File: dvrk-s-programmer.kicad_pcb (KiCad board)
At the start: 4 copper layers, 85.5 x 53 mm, 20 parts, among them J2 Conn_01x04, J3 Conn_02x05_Odd_Even, SW1 SW_SPDT, U1 STM32F103C8Tx, U3 XKTF-015-N

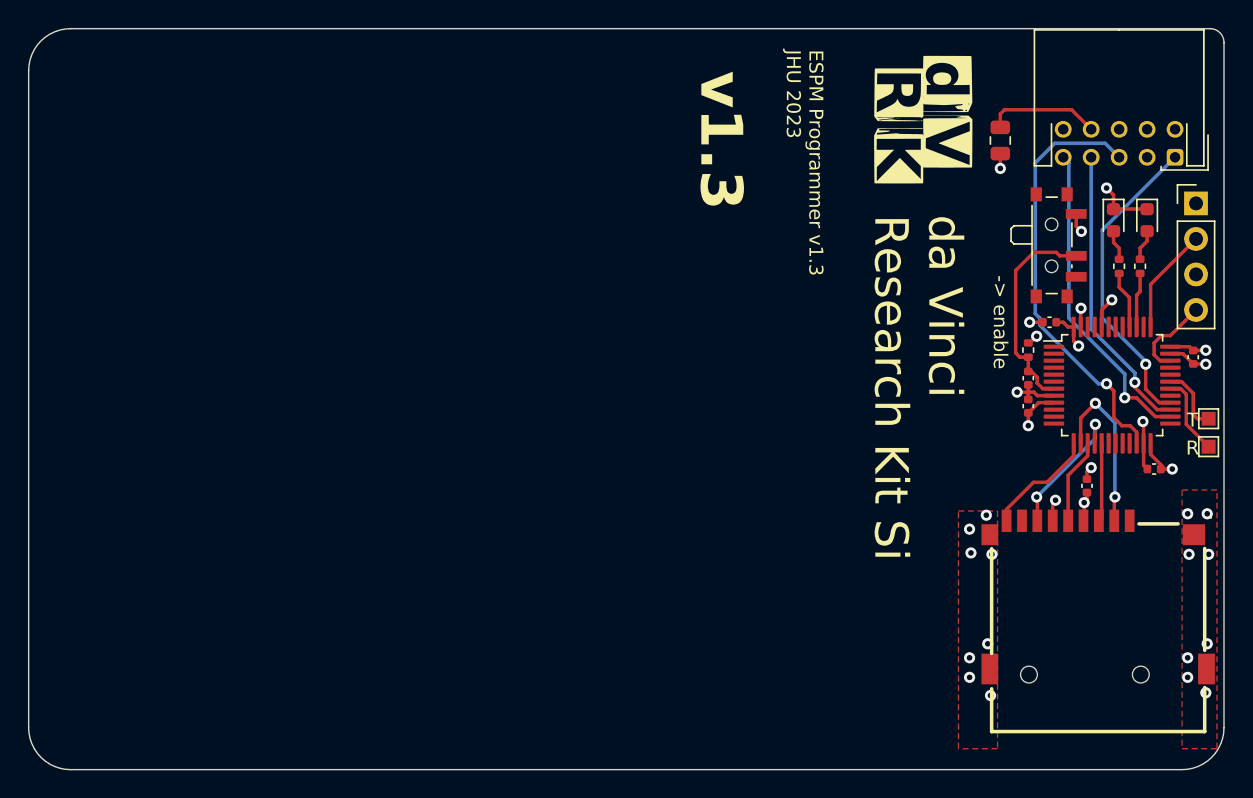
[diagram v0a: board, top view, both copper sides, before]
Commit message: added led array. changed microcontroller.
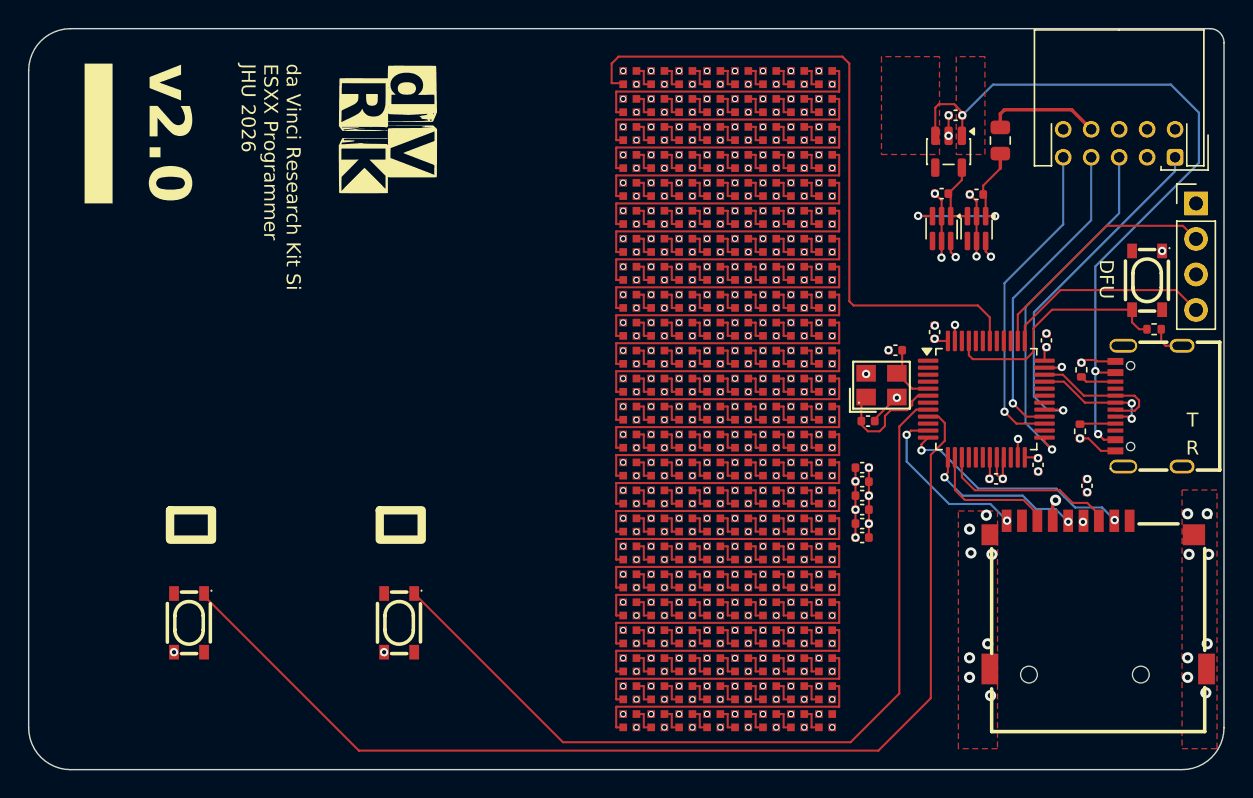
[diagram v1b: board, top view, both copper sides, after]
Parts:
- removed D1, D2: LED, LED_SMD:LED_0603_1608Metric
- removed R2, R3: 2.61k, Resistor_SMD:R_0402_1005Metric
- removed SW1: SW_SPDT, Button_Switch_SMD:SW_SPDT_PCM12
- removed TP1, TP2: TestPoint, TestPoint:TestPoint_Pad_1.0x1.0mm
- removed the U1 at (191.0, 137.0)
- added C11: 1uF, Capacitor_SMD:C_0402_1005Metric, F.Cu at (173.1, 142.9)
- added C12: 1uF, Capacitor_SMD:C_0402_1005Metric, F.Cu at (173.1, 143.9)
- added C13: 1uF, Capacitor_SMD:C_0402_1005Metric, F.Cu at (173.1, 144.9)
- added C14: 1uF, Capacitor_SMD:C_0402_1005Metric, F.Cu at (173.1, 145.9)
- added C15: 1uF, Capacitor_SMD:C_0402_1005Metric, F.Cu at (173.1, 146.9)
- added C16: 1uF, Capacitor_SMD:C_0402_1005Metric, F.Cu at (173.1, 147.9)
- added C2: 10pf, Capacitor_SMD:C_0402_1005Metric, F.Cu at (173.5, 139.6)
- added C5: 1uf, Capacitor_SMD:C_0402_1005Metric, F.Cu at (179.8, 117.7)
- added C8: 1uf, Capacitor_SMD:C_0402_1005Metric, F.Cu at (181.3, 123.4)
- added C9: 1uf, Capacitor_SMD:C_0402_1005Metric, F.Cu at (178.8, 123.3)
- added D10: SK6805-EC15, led-array-generator:SK6805-EC15, F.Cu at (156.5, 129.0)
- added D100: SK6805-EC15, led-array-generator:SK6805-EC15, F.Cu at (164.5, 117.0)
- added D101: SK6805-EC15, led-array-generator:SK6805-EC15, F.Cu at (164.5, 119.0)
- added D102: SK6805-EC15, led-array-generator:SK6805-EC15, F.Cu at (164.5, 121.0)
- added D103: SK6805-EC15, led-array-generator:SK6805-EC15, F.Cu at (164.5, 123.0)
- added D104: SK6805-EC15, led-array-generator:SK6805-EC15, F.Cu at (164.5, 125.0)
- added D105: SK6805-EC15, led-array-generator:SK6805-EC15, F.Cu at (164.5, 127.0)
- added D106: SK6805-EC15, led-array-generator:SK6805-EC15, F.Cu at (164.5, 129.0)
- added D107: SK6805-EC15, led-array-generator:SK6805-EC15, F.Cu at (164.5, 131.0)
- added D108: SK6805-EC15, led-array-generator:SK6805-EC15, F.Cu at (164.5, 133.0)
- added D109: SK6805-EC15, led-array-generator:SK6805-EC15, F.Cu at (164.5, 135.0)
- added D11: SK6805-EC15, led-array-generator:SK6805-EC15, F.Cu at (156.5, 131.0)
- added D110: SK6805-EC15, led-array-generator:SK6805-EC15, F.Cu at (164.5, 137.0)
- added D111: SK6805-EC15, led-array-generator:SK6805-EC15, F.Cu at (164.5, 139.0)
- added D112: SK6805-EC15, led-array-generator:SK6805-EC15, F.Cu at (164.5, 141.0)
- added D113: SK6805-EC15, led-array-generator:SK6805-EC15, F.Cu at (164.5, 143.0)
- added D114: SK6805-EC15, led-array-generator:SK6805-EC15, F.Cu at (164.5, 145.0)
- added D115: SK6805-EC15, led-array-generator:SK6805-EC15, F.Cu at (164.5, 147.0)
- added D116: SK6805-EC15, led-array-generator:SK6805-EC15, F.Cu at (164.5, 149.0)
- added D117: SK6805-EC15, led-array-generator:SK6805-EC15, F.Cu at (164.5, 151.0)
- added D118: SK6805-EC15, led-array-generator:SK6805-EC15, F.Cu at (164.5, 153.0)
- added D119: SK6805-EC15, led-array-generator:SK6805-EC15, F.Cu at (164.5, 155.0)
- added D12: SK6805-EC15, led-array-generator:SK6805-EC15, F.Cu at (156.5, 133.0)
- added D120: SK6805-EC15, led-array-generator:SK6805-EC15, F.Cu at (164.5, 157.0)
- added D121: SK6805-EC15, led-array-generator:SK6805-EC15, F.Cu at (164.5, 159.0)
- added D122: SK6805-EC15, led-array-generator:SK6805-EC15, F.Cu at (164.5, 161.0)
- added D123: SK6805-EC15, led-array-generator:SK6805-EC15, F.Cu at (166.5, 115.0)
- added D124: SK6805-EC15, led-array-generator:SK6805-EC15, F.Cu at (166.5, 117.0)
- added D125: SK6805-EC15, led-array-generator:SK6805-EC15, F.Cu at (166.5, 119.0)
- added D126: SK6805-EC15, led-array-generator:SK6805-EC15, F.Cu at (166.5, 121.0)
- added D127: SK6805-EC15, led-array-generator:SK6805-EC15, F.Cu at (166.5, 123.0)
- added D128: SK6805-EC15, led-array-generator:SK6805-EC15, F.Cu at (166.5, 125.0)
- added D129: SK6805-EC15, led-array-generator:SK6805-EC15, F.Cu at (166.5, 127.0)
- added D13: SK6805-EC15, led-array-generator:SK6805-EC15, F.Cu at (156.5, 135.0)
- added D130: SK6805-EC15, led-array-generator:SK6805-EC15, F.Cu at (166.5, 129.0)
- added D131: SK6805-EC15, led-array-generator:SK6805-EC15, F.Cu at (166.5, 131.0)
- added D132: SK6805-EC15, led-array-generator:SK6805-EC15, F.Cu at (166.5, 133.0)
- added D133: SK6805-EC15, led-array-generator:SK6805-EC15, F.Cu at (166.5, 135.0)
- added D134: SK6805-EC15, led-array-generator:SK6805-EC15, F.Cu at (166.5, 137.0)
- added D135: SK6805-EC15, led-array-generator:SK6805-EC15, F.Cu at (166.5, 139.0)
- added D136: SK6805-EC15, led-array-generator:SK6805-EC15, F.Cu at (166.5, 141.0)
- added D137: SK6805-EC15, led-array-generator:SK6805-EC15, F.Cu at (166.5, 143.0)
- added D138: SK6805-EC15, led-array-generator:SK6805-EC15, F.Cu at (166.5, 145.0)
- added D139: SK6805-EC15, led-array-generator:SK6805-EC15, F.Cu at (166.5, 147.0)
- added D14: SK6805-EC15, led-array-generator:SK6805-EC15, F.Cu at (156.5, 137.0)
- added D140: SK6805-EC15, led-array-generator:SK6805-EC15, F.Cu at (166.5, 149.0)
- added D141: SK6805-EC15, led-array-generator:SK6805-EC15, F.Cu at (166.5, 151.0)
- added D142: SK6805-EC15, led-array-generator:SK6805-EC15, F.Cu at (166.5, 153.0)
- added D143: SK6805-EC15, led-array-generator:SK6805-EC15, F.Cu at (166.5, 155.0)
- added D144: SK6805-EC15, led-array-generator:SK6805-EC15, F.Cu at (166.5, 157.0)
- added D145: SK6805-EC15, led-array-generator:SK6805-EC15, F.Cu at (166.5, 159.0)
- added D146: SK6805-EC15, led-array-generator:SK6805-EC15, F.Cu at (166.5, 161.0)
- added D147: SK6805-EC15, led-array-generator:SK6805-EC15, F.Cu at (168.5, 115.0)
- added D148: SK6805-EC15, led-array-generator:SK6805-EC15, F.Cu at (168.5, 117.0)
- added D149: SK6805-EC15, led-array-generator:SK6805-EC15, F.Cu at (168.5, 119.0)
- added D15: SK6805-EC15, led-array-generator:SK6805-EC15, F.Cu at (156.5, 139.0)
- added D150: SK6805-EC15, led-array-generator:SK6805-EC15, F.Cu at (168.5, 121.0)
- added D151: SK6805-EC15, led-array-generator:SK6805-EC15, F.Cu at (168.5, 123.0)
- added D152: SK6805-EC15, led-array-generator:SK6805-EC15, F.Cu at (168.5, 125.0)
- added D153: SK6805-EC15, led-array-generator:SK6805-EC15, F.Cu at (168.5, 127.0)
- added D154: SK6805-EC15, led-array-generator:SK6805-EC15, F.Cu at (168.5, 129.0)
- added D155: SK6805-EC15, led-array-generator:SK6805-EC15, F.Cu at (168.5, 131.0)
- added D156: SK6805-EC15, led-array-generator:SK6805-EC15, F.Cu at (168.5, 133.0)
- added D157: SK6805-EC15, led-array-generator:SK6805-EC15, F.Cu at (168.5, 135.0)
- added D158: SK6805-EC15, led-array-generator:SK6805-EC15, F.Cu at (168.5, 137.0)
- added D159: SK6805-EC15, led-array-generator:SK6805-EC15, F.Cu at (168.5, 139.0)
- added D16: SK6805-EC15, led-array-generator:SK6805-EC15, F.Cu at (156.5, 141.0)
- added D160: SK6805-EC15, led-array-generator:SK6805-EC15, F.Cu at (168.5, 141.0)
- added D161: SK6805-EC15, led-array-generator:SK6805-EC15, F.Cu at (168.5, 143.0)
- added D162: SK6805-EC15, led-array-generator:SK6805-EC15, F.Cu at (168.5, 145.0)
- added D163: SK6805-EC15, led-array-generator:SK6805-EC15, F.Cu at (168.5, 147.0)
- added D164: SK6805-EC15, led-array-generator:SK6805-EC15, F.Cu at (168.5, 149.0)
- added D165: SK6805-EC15, led-array-generator:SK6805-EC15, F.Cu at (168.5, 151.0)
- added D166: SK6805-EC15, led-array-generator:SK6805-EC15, F.Cu at (168.5, 153.0)
- added D167: SK6805-EC15, led-array-generator:SK6805-EC15, F.Cu at (168.5, 155.0)
- added D168: SK6805-EC15, led-array-generator:SK6805-EC15, F.Cu at (168.5, 157.0)
- added D169: SK6805-EC15, led-array-generator:SK6805-EC15, F.Cu at (168.5, 159.0)
- added D17: SK6805-EC15, led-array-generator:SK6805-EC15, F.Cu at (156.5, 143.0)
- added D170: SK6805-EC15, led-array-generator:SK6805-EC15, F.Cu at (168.5, 161.0)
- added D171: SK6805-EC15, led-array-generator:SK6805-EC15, F.Cu at (170.5, 115.0)
- added D172: SK6805-EC15, led-array-generator:SK6805-EC15, F.Cu at (170.5, 117.0)
- added D173: SK6805-EC15, led-array-generator:SK6805-EC15, F.Cu at (170.5, 119.0)
- added D174: SK6805-EC15, led-array-generator:SK6805-EC15, F.Cu at (170.5, 121.0)
- added D175: SK6805-EC15, led-array-generator:SK6805-EC15, F.Cu at (170.5, 123.0)
- added D176: SK6805-EC15, led-array-generator:SK6805-EC15, F.Cu at (170.5, 125.0)
- added D177: SK6805-EC15, led-array-generator:SK6805-EC15, F.Cu at (170.5, 127.0)
- added D178: SK6805-EC15, led-array-generator:SK6805-EC15, F.Cu at (170.5, 129.0)
- added D179: SK6805-EC15, led-array-generator:SK6805-EC15, F.Cu at (170.5, 131.0)
- added D18: SK6805-EC15, led-array-generator:SK6805-EC15, F.Cu at (156.5, 145.0)
- added D180: SK6805-EC15, led-array-generator:SK6805-EC15, F.Cu at (170.5, 133.0)
- added D181: SK6805-EC15, led-array-generator:SK6805-EC15, F.Cu at (170.5, 135.0)
- added D182: SK6805-EC15, led-array-generator:SK6805-EC15, F.Cu at (170.5, 137.0)
- added D183: SK6805-EC15, led-array-generator:SK6805-EC15, F.Cu at (170.5, 139.0)
- added D184: SK6805-EC15, led-array-generator:SK6805-EC15, F.Cu at (170.5, 141.0)
- added D185: SK6805-EC15, led-array-generator:SK6805-EC15, F.Cu at (170.5, 143.0)
- added D186: SK6805-EC15, led-array-generator:SK6805-EC15, F.Cu at (170.5, 145.0)
- added D187: SK6805-EC15, led-array-generator:SK6805-EC15, F.Cu at (170.5, 147.0)
- added D188: SK6805-EC15, led-array-generator:SK6805-EC15, F.Cu at (170.5, 149.0)
- added D189: SK6805-EC15, led-array-generator:SK6805-EC15, F.Cu at (170.5, 151.0)
- added D19: SK6805-EC15, led-array-generator:SK6805-EC15, F.Cu at (156.5, 147.0)
- added D190: SK6805-EC15, led-array-generator:SK6805-EC15, F.Cu at (170.5, 153.0)
- added D191: SK6805-EC15, led-array-generator:SK6805-EC15, F.Cu at (170.5, 155.0)
- added D192: SK6805-EC15, led-array-generator:SK6805-EC15, F.Cu at (170.5, 157.0)
- added D193: SK6805-EC15, led-array-generator:SK6805-EC15, F.Cu at (170.5, 159.0)
- added D194: SK6805-EC15, led-array-generator:SK6805-EC15, F.Cu at (170.5, 161.0)
- added D20: SK6805-EC15, led-array-generator:SK6805-EC15, F.Cu at (156.5, 149.0)
- added D21: SK6805-EC15, led-array-generator:SK6805-EC15, F.Cu at (156.5, 151.0)
- added D22: SK6805-EC15, led-array-generator:SK6805-EC15, F.Cu at (156.5, 153.0)
- added D23: SK6805-EC15, led-array-generator:SK6805-EC15, F.Cu at (156.5, 155.0)
- added D24: SK6805-EC15, led-array-generator:SK6805-EC15, F.Cu at (156.5, 157.0)
- added D25: SK6805-EC15, led-array-generator:SK6805-EC15, F.Cu at (156.5, 159.0)
- added D26: SK6805-EC15, led-array-generator:SK6805-EC15, F.Cu at (156.5, 161.0)
- added D27: SK6805-EC15, led-array-generator:SK6805-EC15, F.Cu at (158.5, 115.0)
- added D28: SK6805-EC15, led-array-generator:SK6805-EC15, F.Cu at (158.5, 117.0)
- added D29: SK6805-EC15, led-array-generator:SK6805-EC15, F.Cu at (158.5, 119.0)
- added D3: SK6805-EC15, led-array-generator:SK6805-EC15, F.Cu at (156.5, 115.0)
- added D30: SK6805-EC15, led-array-generator:SK6805-EC15, F.Cu at (158.5, 121.0)
- added D31: SK6805-EC15, led-array-generator:SK6805-EC15, F.Cu at (158.5, 123.0)
- added D32: SK6805-EC15, led-array-generator:SK6805-EC15, F.Cu at (158.5, 125.0)
- added D33: SK6805-EC15, led-array-generator:SK6805-EC15, F.Cu at (158.5, 127.0)
- added D34: SK6805-EC15, led-array-generator:SK6805-EC15, F.Cu at (158.5, 129.0)
- added D35: SK6805-EC15, led-array-generator:SK6805-EC15, F.Cu at (158.5, 131.0)
- added D36: SK6805-EC15, led-array-generator:SK6805-EC15, F.Cu at (158.5, 133.0)
- added D37: SK6805-EC15, led-array-generator:SK6805-EC15, F.Cu at (158.5, 135.0)
- added D38: SK6805-EC15, led-array-generator:SK6805-EC15, F.Cu at (158.5, 137.0)
- added D39: SK6805-EC15, led-array-generator:SK6805-EC15, F.Cu at (158.5, 139.0)
- added D4: SK6805-EC15, led-array-generator:SK6805-EC15, F.Cu at (156.5, 117.0)
- added D40: SK6805-EC15, led-array-generator:SK6805-EC15, F.Cu at (158.5, 141.0)
- added D41: SK6805-EC15, led-array-generator:SK6805-EC15, F.Cu at (158.5, 143.0)
- added D42: SK6805-EC15, led-array-generator:SK6805-EC15, F.Cu at (158.5, 145.0)
- added D43: SK6805-EC15, led-array-generator:SK6805-EC15, F.Cu at (158.5, 147.0)
- added D44: SK6805-EC15, led-array-generator:SK6805-EC15, F.Cu at (158.5, 149.0)
- added D45: SK6805-EC15, led-array-generator:SK6805-EC15, F.Cu at (158.5, 151.0)
- added D46: SK6805-EC15, led-array-generator:SK6805-EC15, F.Cu at (158.5, 153.0)
- added D47: SK6805-EC15, led-array-generator:SK6805-EC15, F.Cu at (158.5, 155.0)
- added D48: SK6805-EC15, led-array-generator:SK6805-EC15, F.Cu at (158.5, 157.0)
- added D49: SK6805-EC15, led-array-generator:SK6805-EC15, F.Cu at (158.5, 159.0)
- added D5: SK6805-EC15, led-array-generator:SK6805-EC15, F.Cu at (156.5, 119.0)
- added D50: SK6805-EC15, led-array-generator:SK6805-EC15, F.Cu at (158.5, 161.0)
- added D51: SK6805-EC15, led-array-generator:SK6805-EC15, F.Cu at (160.5, 115.0)
- added D52: SK6805-EC15, led-array-generator:SK6805-EC15, F.Cu at (160.5, 117.0)
- added D53: SK6805-EC15, led-array-generator:SK6805-EC15, F.Cu at (160.5, 119.0)
- added D54: SK6805-EC15, led-array-generator:SK6805-EC15, F.Cu at (160.5, 121.0)
- added D55: SK6805-EC15, led-array-generator:SK6805-EC15, F.Cu at (160.5, 123.0)
- added D56: SK6805-EC15, led-array-generator:SK6805-EC15, F.Cu at (160.5, 125.0)
- added D57: SK6805-EC15, led-array-generator:SK6805-EC15, F.Cu at (160.5, 127.0)
- added D58: SK6805-EC15, led-array-generator:SK6805-EC15, F.Cu at (160.5, 129.0)
- added D59: SK6805-EC15, led-array-generator:SK6805-EC15, F.Cu at (160.5, 131.0)
- added D6: SK6805-EC15, led-array-generator:SK6805-EC15, F.Cu at (156.5, 121.0)
- added D60: SK6805-EC15, led-array-generator:SK6805-EC15, F.Cu at (160.5, 133.0)
- added D61: SK6805-EC15, led-array-generator:SK6805-EC15, F.Cu at (160.5, 135.0)
- added D62: SK6805-EC15, led-array-generator:SK6805-EC15, F.Cu at (160.5, 137.0)
- added D63: SK6805-EC15, led-array-generator:SK6805-EC15, F.Cu at (160.5, 139.0)
- added D64: SK6805-EC15, led-array-generator:SK6805-EC15, F.Cu at (160.5, 141.0)
- added D65: SK6805-EC15, led-array-generator:SK6805-EC15, F.Cu at (160.5, 143.0)
- added D66: SK6805-EC15, led-array-generator:SK6805-EC15, F.Cu at (160.5, 145.0)
- added D67: SK6805-EC15, led-array-generator:SK6805-EC15, F.Cu at (160.5, 147.0)
- added D68: SK6805-EC15, led-array-generator:SK6805-EC15, F.Cu at (160.5, 149.0)
- added D69: SK6805-EC15, led-array-generator:SK6805-EC15, F.Cu at (160.5, 151.0)
- added D7: SK6805-EC15, led-array-generator:SK6805-EC15, F.Cu at (156.5, 123.0)
- added D70: SK6805-EC15, led-array-generator:SK6805-EC15, F.Cu at (160.5, 153.0)
- added D71: SK6805-EC15, led-array-generator:SK6805-EC15, F.Cu at (160.5, 155.0)
- added D72: SK6805-EC15, led-array-generator:SK6805-EC15, F.Cu at (160.5, 157.0)
- added D73: SK6805-EC15, led-array-generator:SK6805-EC15, F.Cu at (160.5, 159.0)
- added D74: SK6805-EC15, led-array-generator:SK6805-EC15, F.Cu at (160.5, 161.0)
- added D75: SK6805-EC15, led-array-generator:SK6805-EC15, F.Cu at (162.5, 115.0)
- added D76: SK6805-EC15, led-array-generator:SK6805-EC15, F.Cu at (162.5, 117.0)
- added D77: SK6805-EC15, led-array-generator:SK6805-EC15, F.Cu at (162.5, 119.0)
- added D78: SK6805-EC15, led-array-generator:SK6805-EC15, F.Cu at (162.5, 121.0)
- added D79: SK6805-EC15, led-array-generator:SK6805-EC15, F.Cu at (162.5, 123.0)
- added D8: SK6805-EC15, led-array-generator:SK6805-EC15, F.Cu at (156.5, 125.0)
- added D80: SK6805-EC15, led-array-generator:SK6805-EC15, F.Cu at (162.5, 125.0)
- added D81: SK6805-EC15, led-array-generator:SK6805-EC15, F.Cu at (162.5, 127.0)
- added D82: SK6805-EC15, led-array-generator:SK6805-EC15, F.Cu at (162.5, 129.0)
- added D83: SK6805-EC15, led-array-generator:SK6805-EC15, F.Cu at (162.5, 131.0)
- added D84: SK6805-EC15, led-array-generator:SK6805-EC15, F.Cu at (162.5, 133.0)
- added D85: SK6805-EC15, led-array-generator:SK6805-EC15, F.Cu at (162.5, 135.0)
- added D86: SK6805-EC15, led-array-generator:SK6805-EC15, F.Cu at (162.5, 137.0)
- added D87: SK6805-EC15, led-array-generator:SK6805-EC15, F.Cu at (162.5, 139.0)
- added D88: SK6805-EC15, led-array-generator:SK6805-EC15, F.Cu at (162.5, 141.0)
- added D89: SK6805-EC15, led-array-generator:SK6805-EC15, F.Cu at (162.5, 143.0)
- added D9: SK6805-EC15, led-array-generator:SK6805-EC15, F.Cu at (156.5, 127.0)
- added D90: SK6805-EC15, led-array-generator:SK6805-EC15, F.Cu at (162.5, 145.0)
- added D91: SK6805-EC15, led-array-generator:SK6805-EC15, F.Cu at (162.5, 147.0)
- added D92: SK6805-EC15, led-array-generator:SK6805-EC15, F.Cu at (162.5, 149.0)
- added D93: SK6805-EC15, led-array-generator:SK6805-EC15, F.Cu at (162.5, 151.0)
- added D94: SK6805-EC15, led-array-generator:SK6805-EC15, F.Cu at (162.5, 153.0)
- added D95: SK6805-EC15, led-array-generator:SK6805-EC15, F.Cu at (162.5, 155.0)
- added D96: SK6805-EC15, led-array-generator:SK6805-EC15, F.Cu at (162.5, 157.0)
- added D97: SK6805-EC15, led-array-generator:SK6805-EC15, F.Cu at (162.5, 159.0)
- added D98: SK6805-EC15, led-array-generator:SK6805-EC15, F.Cu at (162.5, 161.0)
- added D99: SK6805-EC15, led-array-generator:SK6805-EC15, F.Cu at (164.5, 115.0)
- added R4: 5.1k, Resistor_SMD:R_0402_1005Metric, F.Cu at (188.8, 135.9)
- added R5: 5.1k, Resistor_SMD:R_0402_1005Metric, F.Cu at (188.7, 140.3)
- added U2: SKRPABE010, footprint:KEY-SMD_4P-L4.2-W3.2-P2.20-LS4.6, F.Cu at (193.5, 129.5)
- added U3: STM32G474CETx, Package_QFP:LQFP-48_7x7mm_P0.5mm, F.Cu at (182.0, 138.0)
- added U4: USB-TYPE-C-019, footprint:TYPE-C-SMD_HX-TYPE-C-16PIN, F.Cu at (193.6, 138.5)
- added U5: LP5907MFX-3.3, Package_TO_SOT_SMD:SOT-23-5, F.Cu at (179.3, 120.3)
- added U6: LM66100DCK, Package_TO_SOT_SMD:SOT-363_SC-70-6, F.Cu at (181.3, 125.8)
- added U7: LM66100DCK, Package_TO_SOT_SMD:SOT-363_SC-70-6, F.Cu at (178.8, 125.8)
- added U8: SKRPABE010, footprint:KEY-SMD_4P-L4.2-W3.2-P2.20-LS4.6, F.Cu at (140.0, 154.0)
- added U9: SKRPABE010, footprint:KEY-SMD_4P-L4.2-W3.2-P2.20-LS4.6, F.Cu at (125.0, 154.0)
- added X1: L327S080D11L, footprint:CRYSTAL-SMD_4P-L3.2-W2.5-BL, F.Cu at (174.5, 137.0)
- C1: value 100nF -> 10pf
- R1: value 100k -> 10k
- moved G*** 38.3 mm to (139.2, 118.7)
- moved C3 18.6 mm to (178.3, 133.2), turned to 90 degrees
- moved C10 11.3 mm to (182.7, 143.7)
- moved C1 9.71 mm to (175.5, 134.5), turned to 0 degrees
- moved R1 9.12 mm to (194.0, 133.0), turned to 180 degrees
- moved C4 4.26 mm to (185.7, 142.7), turned to -90 degrees
- moved C6 1.32 mm to (186.3, 133.8), turned to 90 degrees
- renumbered C6 to C10, C2 to C3, C3 to C4, C4 to C6, C5 to C7, J3 to J1, U3 to U1
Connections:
- C1 pad 1: Net-(SW1-B) -> GND
- C1 pad 2: GND -> Net-(U3-PF0)
- F1 pad 2: VDD -> /TARGET_3.3
- R1 pad 1: VDD -> GND
- R1 pad 2: Net-(SW1-B) -> /BOOT0
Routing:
- net /button_go: track 0.00 -> 79.8 mm
- net /button_next: track 0.00 -> 62.2 mm
- net VBUS: track 0.00 -> 53.7 mm, vias 0 -> 3
- net /LED: track 0.00 -> 48.9 mm
- net Net-(D193-DOUT): track 0.00 -> 19.9 mm
- net Net-(D192-DOUT): track 0.00 -> 19.9 mm
- net Net-(D191-DOUT): track 0.00 -> 19.9 mm
- net Net-(D190-DOUT): track 0.00 -> 19.9 mm
- net Net-(D189-DOUT): track 0.00 -> 19.9 mm
- net Net-(D188-DOUT): track 0.00 -> 19.9 mm
- net Net-(D187-DOUT): track 0.00 -> 19.9 mm
- net Net-(D186-DOUT): track 0.00 -> 19.9 mm
- net Net-(D18-DIN): track 0.00 -> 19.9 mm
- net Net-(D176-DOUT): track 0.00 -> 19.9 mm
- net Net-(D175-DOUT): track 0.00 -> 19.9 mm
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- added copper zone on F.Cu, net VBUS
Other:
- board text added: ".LED"
- board text added: "DFU"
- board text added: "da Vinci Research Kit Si ESXX Programmer JHU 2026"
- board text added: "v2.0"
- board text added: ""
- board text added: ""
- board text removed: "-> enable"
- board text removed: "ESPM Programmer v1.3 JHU 2023"
- board text removed: "da Vinci Research Kit Si"
- board text removed: "reprogram"
- board text removed: "v1.3"
